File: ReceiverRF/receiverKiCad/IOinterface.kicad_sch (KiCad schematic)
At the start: 23 parts

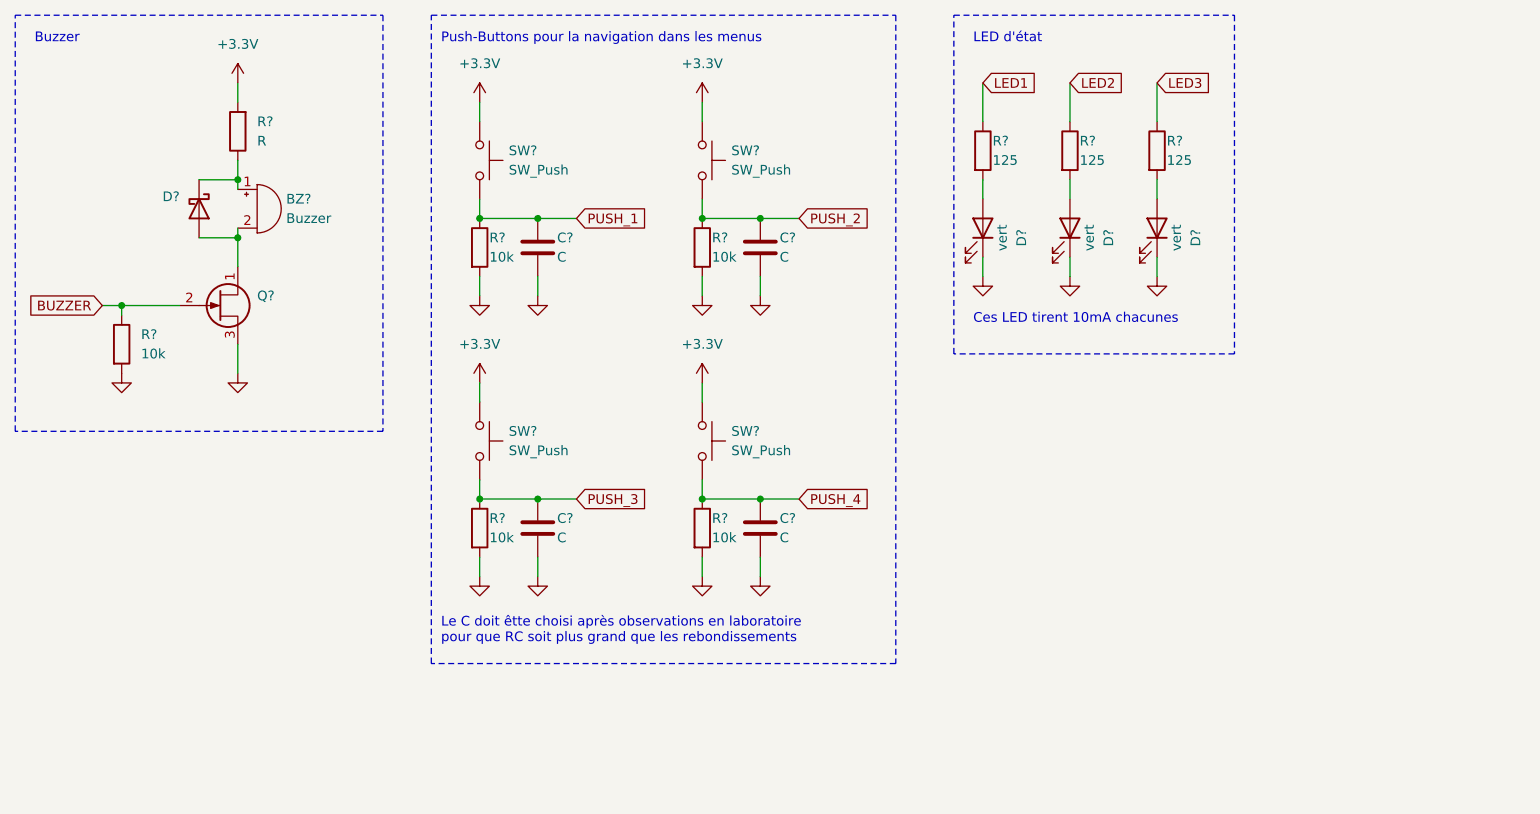
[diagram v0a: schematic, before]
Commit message: Changement régulateurs, meilleur circuit debouncing boutons, documentation
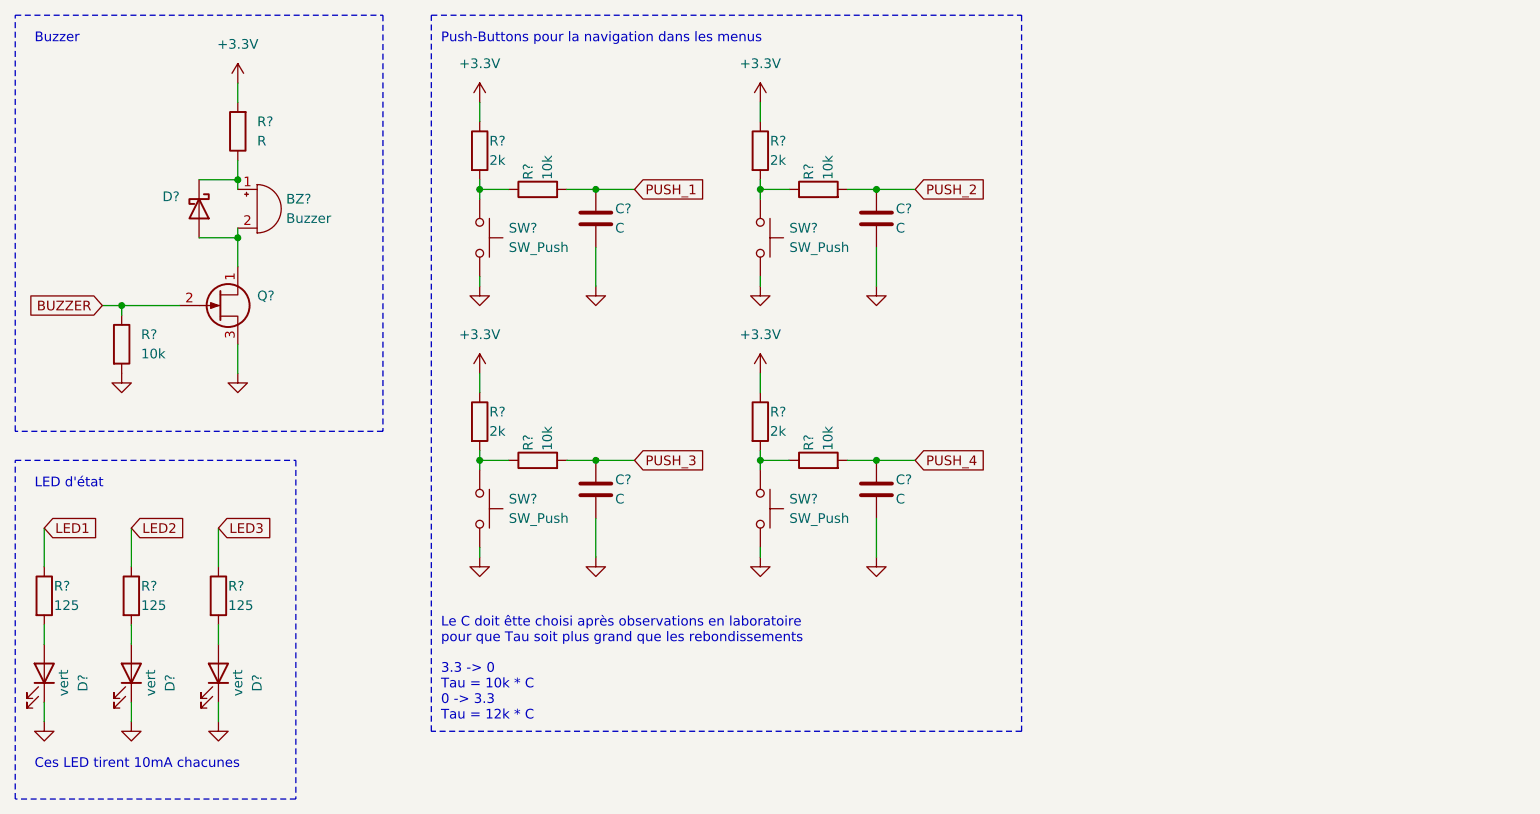
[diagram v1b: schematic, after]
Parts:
- removed C? (x3): C, symbol Device:C
- removed R? (x3): 10k, symbol Device:R
- removed SW? (x3): SW_Push, symbol Switch:SW_Push
- added C? (x3): C, symbol Device:C
- added R? (x4): 10k, symbol Device:R
- added R? (x3): 2k, symbol Device:R
- added SW? (x3): SW_Push, symbol Switch:SW_Push
- R?: value 10k -> 2k
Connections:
- net +3.3V: now also R?.1, R?.1, R?.1, R?.1; no longer SW?.1
- net GND: now also SW?.2, C?.2, C?.2, C?.2, SW?.2, SW?.2, SW?.2; no longer R?.2
- net PUSH_1: now also R?.2; no longer R?.1, SW?.2
- net PUSH_2: now also C?.1, R?.2
- net PUSH_3: now also C?.1, R?.2
- net PUSH_4: now also C?.1, R?.2
- new net: R?.1, R?.2, SW?.1 (x4)
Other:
- note added: "3.3 -> 0 Tau = 10k * C 0 -> 3.3 Tau = 12k * C"
- note added: "Le C doit êtte choisi après observations en laboratoire pour que Tau soit plus grand que les rebondissements"
- note removed: "Le C doit êtte choisi après observations en laboratoire pour que RC soit plus grand que les rebondissements"
- moved on the sheet: C?, D?, R?, SW?

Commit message: Corrige path footprints
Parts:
- BZ?: footprint footprint-receiver:SMTB-0927-TW-R_PUI -> (none)
- D? (x3): footprint footprint-receiver:LTST-C170GKT -> Footprints:LTST-C170GKT
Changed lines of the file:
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@@
 			)
 		)
-		(property "Footprint" "footprint-receiver:LTST-C170GKT"
+		(property "Footprint" "Footprints:LTST-C170GKT"
 			(at 49.53 107.95 0)
 			(effects
@@
 			)
 		)
-		(property "Footprint" "footprint-receiver:SMTB-0927-TW-R_PUI"
+		(property "Footprint" ""
 			(at 53.975 44.45 90)
 			(effects
@@
 			)
 		)
-		(property "Footprint" "footprint-receiver:LTST-C170GKT"
+		(property "Footprint" "Footprints:LTST-C170GKT"
 			(at 38.1 107.95 0)
 			(effects
@@
 			)
 		)
-		(property "Footprint" "footprint-receiver:LTST-C170GKT"
+		(property "Footprint" "Footprints:LTST-C170GKT"
 			(at 26.67 107.95 0)
 			(effects

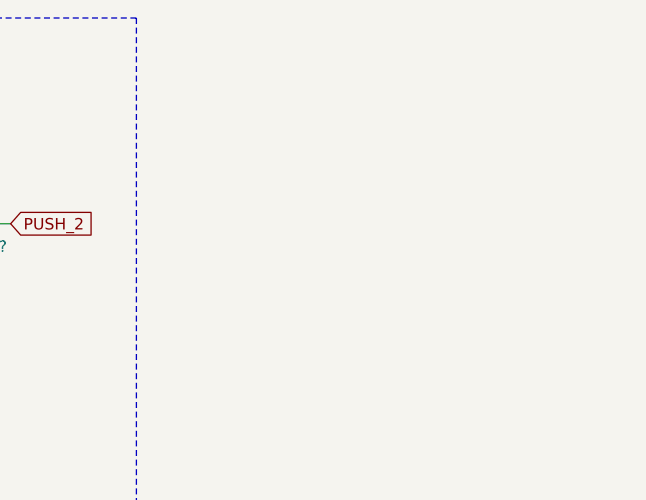
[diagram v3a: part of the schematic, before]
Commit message: Ajout footprint et circuit pour potentiomètre volume, push button, on/off switch
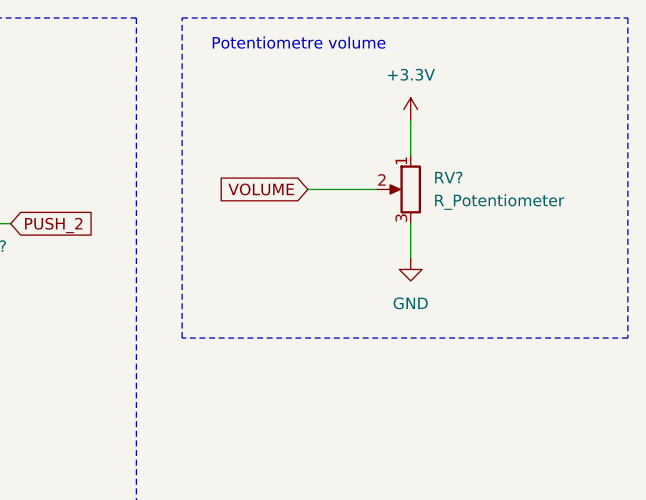
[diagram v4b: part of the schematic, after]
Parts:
- removed SW? (x3): SW_Push, symbol Switch:SW_Push
- added RV?: R_Potentiometer, Footprints:Potentiometer_Alps_RK09K_Single_Vertical, symbol Device:R_Potentiometer
- added SW? (x3): SW_Push, Footprints:SW_PUSH_6mm_H4.3mm, symbol Switch:SW_Push
- SW?: footprint (none) -> Footprints:SW_PUSH_6mm_H4.3mm
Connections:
- net +3.3V: now also RV?.1
- net GND: now also RV?.3, SW?.2, SW?.2, SW?.2
- net at R?.1, R?.2: now also SW?.1 (x3)
- new net VOLUME: RV?.2
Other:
- note added: "Potentiometre volume"

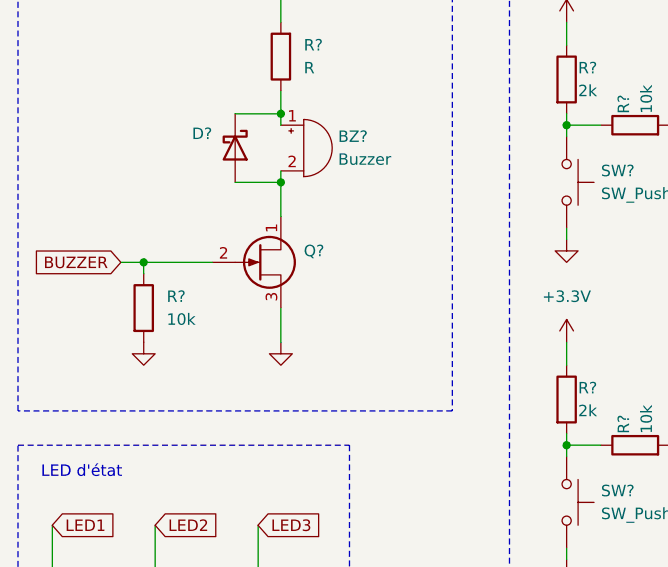
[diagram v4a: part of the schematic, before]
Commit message: Buzzer et diode. Toutes les pièces importantes sont choisies et footprint
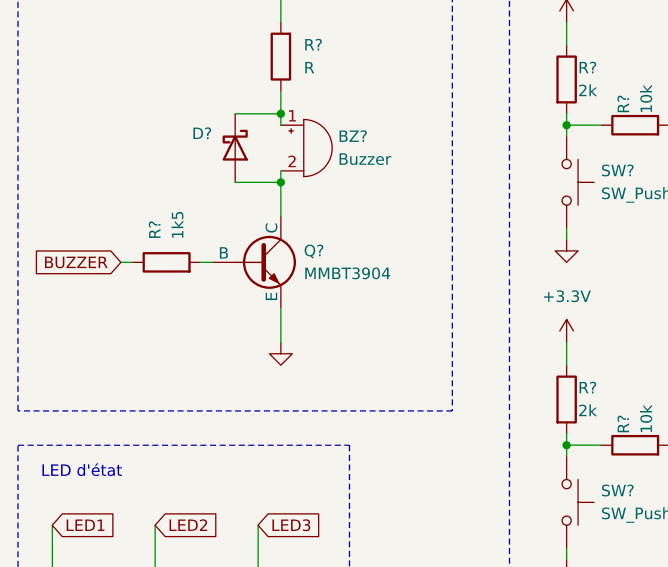
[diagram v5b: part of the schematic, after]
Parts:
- removed Q?: ~, symbol Transistor_FET:2N3819
- added Q?: MMBT3904, Footprints:SOT-23, symbol Simulation_SPICE:NPN
- BZ?: footprint (none) -> Footprints:Buzzer_D14mm_H7mm_P10mm
- D?: footprint (none) -> Diode_SMD:D_SOD-123
- R?: value 10k -> 1k5
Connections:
- net GND: now also Q?.3 (E); no longer R?.2
- net at BZ?.2 (+), D?.2 (A): now also Q?.1 (C)
- new net: Q?.2 (B), R?.2
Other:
- moved on the sheet: R?
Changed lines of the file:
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@@
 	)
 	(junction
-		(at 36.83 59.69)
-		(diameter 0)
-		(color 0 0 0 0)
-	)
-	(junction
 		(at 52.07 43.18)
 		(diameter 0)
@@
 	(wire
 		(pts
-			(xy 36.83 60.96) (xy 36.83 59.69)
-		)
-		(stroke
-			(width 0)
-			(type default)
-		)
-	)
-	(wire
-		(pts
 			(xy 173.99 40.64) (xy 181.61 40.64)
 		)
@@
 	(wire
 		(pts
-			(xy 36.83 59.69) (xy 44.45 59.69)
-		)
-		(stroke
-			(width 0)
-			(type default)
-		)
-	)
-	(wire
-		(pts
 			(xy 83.82 33.02) (xy 83.82 35.56)
 		)
@@
 	(wire
 		(pts
-			(xy 34.29 59.69) (xy 36.83 59.69)
+			(xy 99.06 44.45) (xy 104.14 44.45)
 		)
 		(stroke
@@
 	(wire
 		(pts
-			(xy 99.06 44.45) (xy 104.14 44.45)
+			(xy 120.65 68.58) (xy 120.65 71.12)
 		)
 		(stroke
@@
 	(wire
 		(pts
-			(xy 120.65 68.58) (xy 120.65 71.12)
+			(xy 83.82 44.45) (xy 83.82 45.72)
 		)
 		(stroke
@@
 	(wire
 		(pts
-			(xy 83.82 44.45) (xy 83.82 45.72)
+			(xy 135.89 52.07) (xy 135.89 57.15)
 		)
 		(stroke
@@
 	(wire
 		(pts
-			(xy 135.89 52.07) (xy 135.89 57.15)
+			(xy 99.06 52.07) (xy 99.06 57.15)
 		)
 		(stroke
@@
 	(wire
 		(pts
-			(xy 99.06 52.07) (xy 99.06 57.15)
+			(xy 34.29 59.69) (xy 35.56 59.69)
 		)
 		(stroke
@@
 	(wire
 		(pts
+			(xy 43.18 59.69) (xy 44.45 59.69)
+		)
+		(stroke
+			(width 0)
+			(type default)
+		)
+	)
+	(wire
+		(pts
 			(xy 120.65 80.01) (xy 120.65 81.28)
 		)
@@
 	)
 	(symbol
-		(lib_id "Transistor_FET:2N3819")
-		(at 49.53 59.69 0)
-		(unit 1)
-		(exclude_from_sim no)
-		(in_bom yes)
-		(on_board yes)
-		(dnp no)
-		(fields_autoplaced yes)
-		(property "Reference" "Q?"
-			(at 54.61 58.42 0)
-			(effects
-				(font
-					(size 1.27 1.27)
-				)
-				(justify left)
-			)
-		)
-		(property "Value" "~"
-			(at 54.61 60.96 0)
-			(effects
-				(font
-					(size 1.27 1.27)
-				)
-				(justify left)
-			)
-		)
-		(property "Footprint" ""
-			(at 54.61 61.595 0)
-			(effects
-				(font
-					(size 1.27 1.27)
-					(italic yes)
-				)
-				(justify left)
-				(hide yes)
-			)
-		)
-		(property "Datasheet" "https://my.centralsemi.com/datasheets/2N3819.PDF"
-			(at 49.53 59.69 0)
-			(effects
-				(font
-					(size 1.27 1.27)
-				)
-				(justify left)
-				(hide yes)
-			)
-		)
-		(property "Description" ""
-			(at 49.53 59.69 0)
-			(effects
-				(font
-					(size 1.27 1.27)
-				)
-				(hide yes)
-			)
-		)
-		(pin "1"
-		)
-		(pin "2"
-		)
-		(pin "3"
-		)
-		(instances
-			(project "receiver"
-				(path "/439ba515-58d4-4b14-87ab-b438dcf423a5/4d4f24f8-ecba-4dd7-9441-941d52592651"
-					(reference "Q?")
-					(unit 1)
-				)
-			)
-		)
-	)
-	(symbol
 		(lib_id "Device:R")
 		(at 52.07 36.83 180)
@@
 			)
 		)
-		(property "Footprint" ""
+		(property "Footprint" "Footprints:Buzzer_D14mm_H7mm_P10mm"
 			(at 53.975 44.45 90)
 			(effects
@@
 			)
 		)
-		(property "Datasheet" "~"
+		(property "Datasheet" "https://www.digikey.com/en/products/detail/pui-audio-inc/SMTB-0927-TW-R/13165907"
 			(at 53.975 44.45 90)
 			(effects
@@
 	(symbol
 		(lib_id "power:GND")
-		(at 36.83 68.58 0)
+		(at 83.82 57.15 0)
 		(unit 1)
 		(exclude_from_sim no)
@@
 		(dnp no)
 		(fields_autoplaced yes)
-		(property "Reference" "#PWR041"
-			(at 36.83 74.93 0)
+		(property "Reference" "#PWR043"
+			(at 83.82 63.5 0)
 			(effects
 				(font
@@
 		)
 		(property "Value" "GND"
-			(at 36.83 73.66 0)
+			(at 83.82 62.23 0)
 			(effects
 				(font
@@
 		)
 		(property "Footprint" ""
-			(at 36.83 68.58 0)
+			(at 83.82 57.15 0)
 			(effects
 				(font
@@
 		)
 		(property "Datasheet" ""
-			(at 36.83 68.58 0)
+			(at 83.82 57.15 0)
 			(effects
 				(font
@@
 		)
 		(property "Description" ""
-			(at 36.83 68.58 0)
+			(at 83.82 57.15 0)
 			(effects
 				(font
@@
 			(project "receiver"
 				(path "/439ba515-58d4-4b14-87ab-b438dcf423a5/4d4f24f8-ecba-4dd7-9441-941d52592651"
-					(reference "#PWR041")
+					(reference "#PWR043")
 					(unit 1)
 				)
@@
 	)
 	(symbol
-		(lib_id "power:GND")
-		(at 83.82 57.15 0)
+		(lib_id "Simulation_SPICE:NPN")
+		(at 49.53 59.69 0)
 		(unit 1)
 		(exclude_from_sim no)
@@
 		(dnp no)
 		(fields_autoplaced yes)
-		(property "Reference" "#PWR043"
-			(at 83.82 63.5 0)
+		(property "Reference" "Q?"
+			(at 54.61 58.4199 0)
+			(effects
+				(font
+					(size 1.27 1.27)
+				)
+				(justify left)
+			)
+		)
+		(property "Value" "MMBT3904"
+			(at 54.61 60.9599 0)
+			(effects
+				(font
+					(size 1.27 1.27)
+				)
+				(justify left)
+			)
+		)
+		(property "Footprint" "Footprints:SOT-23"
+			(at 113.03 59.69 0)
 			(effects
 				(font
@@
 			)
 		)
-		(property "Value" "GND"
-			(at 83.82 62.23 0)
+		(property "Datasheet" "https://www.digikey.ca/en/products/detail/onsemi/MMBT3904LT1G/1139813"
+			(at 113.03 59.69 0)
 			(effects
 				(font
@@
 			)
 		)
-		(property "Footprint" ""
-			(at 83.82 57.15 0)
+		(property "Description" "Bipolar transistor symbol for simulation only, substrate tied to the emitter"
+			(at 49.53 59.69 0)
 			(effects
 				(font
@@
 			)
 		)
-		(property "Datasheet" ""
-			(at 83.82 57.15 0)
+		(property "Sim.Device" "NPN"
+			(at 49.53 59.69 0)
 			(effects
 				(font
@@
 			)
 		)
-		(property "Description" ""
-			(at 83.82 57.15 0)
+		(property "Sim.Type" "GUMMELPOON"
+			(at 49.53 59.69 0)
+			(effects
+				(font
+					(size 1.27 1.27)
+				)
+				(hide yes)
+			)
+		)
+		(property "Sim.Pins" "1=C 2=B 3=E"
+			(at 49.53 59.69 0)
 			(effects
 				(font
@@
 			)
 		)
+		(pin "3"
+		)
 		(pin "1"
 		)
+		(pin "2"
+		)
 		(instances
-			(project "receiver"
+			(project ""
 				(path "/439ba515-58d4-4b14-87ab-b438dcf423a5/4d4f24f8-ecba-4dd7-9441-941d52592651"
-					(reference "#PWR043")
+					(reference "Q?")
 					(unit 1)
 				)
@@
 	(symbol
 		(lib_id "Device:R")
-		(at 36.83 64.77 0)
+		(at 39.37 59.69 90)
 		(unit 1)
 		(exclude_from_sim no)
@@
 		(on_board yes)
 		(dnp no)
-		(fields_autoplaced yes)
 		(property "Reference" "R?"
-			(at 39.37 63.5 0)
+			(at 38.1 57.15 0)
 			(effects
 				(font
@@
 			)
 		)
-		(property "Value" "10k"
-			(at 39.37 66.04 0)
+		(property "Value" "1k5"
+			(at 40.64 57.15 0)
 			(effects
 				(font
@@
 		)
 		(property "Footprint" ""
-			(at 35.052 64.77 90)
+			(at 39.37 61.468 90)
 			(effects
 				(font
@@
 		)
 		(property "Datasheet" "~"
-			(at 36.83 64.77 0)
+			(at 39.37 59.69 0)
 			(effects
 				(font
@@
 		)
 		(property "Description" ""
-			(at 36.83 64.77 0)
+			(at 39.37 59.69 0)
 			(effects
 				(font
@@
 			)
 		)
-		(property "Footprint" ""
+		(property "Footprint" "Diode_SMD:D_SOD-123"
 			(at 42.545 46.99 0)
 			(effects
@@
 			)
 		)
-		(property "Datasheet" "https://www.microsemi.com/document-portal/doc_download/131890-lds-0040-1-datasheet"
+		(property "Datasheet" "https://www.digikey.ca/en/products/detail/onsemi/BAT54T1G/918319"
 			(at 46.99 46.99 0)
 			(effects

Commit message: Identifiants des symboles
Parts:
- BUZ_R1: renamed from R?; value R -> 30R
- gave numbers to parts that had none: 27
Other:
- moved on the sheet: BUT_C1, BUT_C2, BUT_C3, BUT_C4, BUT_R2, BUT_R3, BUT_R4, BUT_R6, BUT_R7, BUT_R8, RV1, SW2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

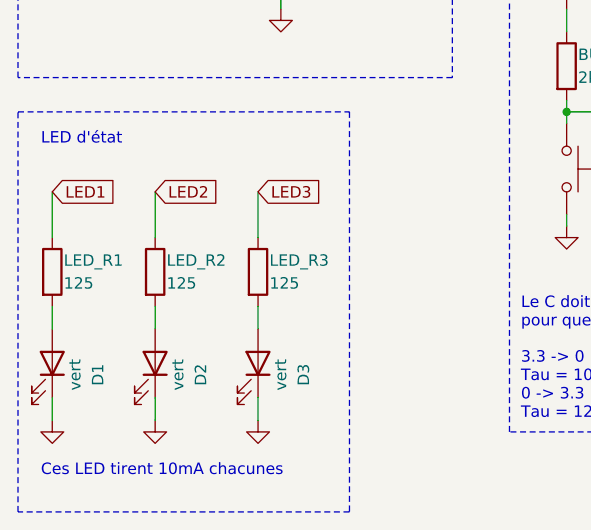
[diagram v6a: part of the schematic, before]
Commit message: Footprint et choix composantes mineures (résistances et condo)
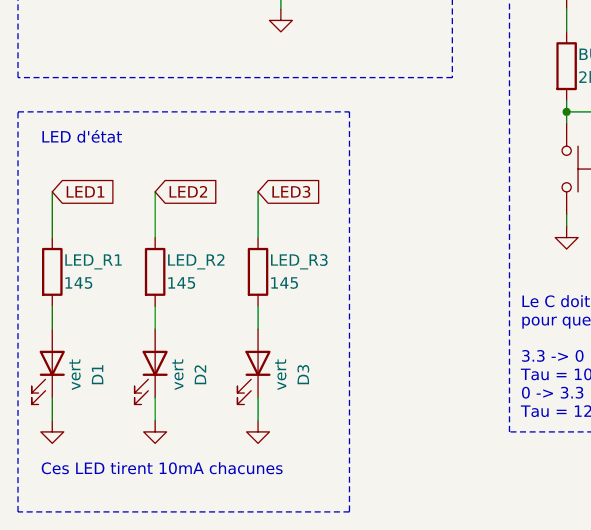
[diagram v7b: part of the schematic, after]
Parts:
- BUT_C1, BUT_C2, BUT_C3, BUT_C4: footprint (none) -> Capacitor_SMD:C_0402_1005Metric
- BUT_R1, BUT_R2, BUT_R5, BUT_R6, BUZ_R1, BUZ_R2: footprint (none) -> Resistor_SMD:R_1206_3216Metric
- BUT_R3, BUT_R4, BUT_R7, BUT_R8: footprint (none) -> Resistor_SMD:R_0402_1005Metric
- LED_R1, LED_R2, LED_R3: value 125 -> 145; footprint (none) -> Resistor_SMD:R_1206_3216Metric
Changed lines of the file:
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@@
 			)
 		)
-		(property "Footprint" ""
+		(property "Footprint" "Resistor_SMD:R_0402_1005Metric"
 			(at 138.43 46.228 90)
 			(effects
@@
 			)
 		)
-		(property "Footprint" ""
+		(property "Footprint" "Resistor_SMD:R_1206_3216Metric"
 			(at 53.848 36.83 90)
 			(effects
@@
 			)
 		)
-		(property "Footprint" ""
+		(property "Footprint" "Capacitor_SMD:C_0402_1005Metric"
 			(at 105.1052 54.61 0)
 			(effects
@@
 			)
 		)
-		(property "Value" "125"
+		(property "Value" "145"
 			(at 39.37 99.06 0)
 			(effects
@@
 			)
 		)
-		(property "Footprint" ""
+		(property "Footprint" "Resistor_SMD:R_1206_3216Metric"
 			(at 36.322 97.79 90)
 			(effects
@@
 			)
 		)
-		(property "Footprint" ""
+		(property "Footprint" "Resistor_SMD:R_0402_1005Metric"
 			(at 96.52 81.788 90)
 			(effects
@@
 			)
 		)
-		(property "Footprint" ""
+		(property "Footprint" "Resistor_SMD:R_0402_1005Metric"
 			(at 138.43 81.788 90)
 			(effects
@@
 			)
 		)
-		(property "Footprint" ""
+		(property "Footprint" "Capacitor_SMD:C_0402_1005Metric"
 			(at 147.0152 90.17 0)
 			(effects
@@
 			)
 		)
-		(property "Footprint" ""
+		(property "Footprint" "Resistor_SMD:R_0402_1005Metric"
 			(at 96.52 46.228 90)
 			(effects
@@
 			)
 		)
-		(property "Footprint" ""
+		(property "Footprint" "Resistor_SMD:R_1206_3216Metric"
 			(at 39.37 61.468 90)
 			(effects
@@
 			)
 		)
-		(property "Footprint" ""
+		(property "Footprint" "Resistor_SMD:R_1206_3216Metric"
 			(at 122.682 39.37 90)
 			(effects
@@
 			)
 		)
-		(property "Footprint" ""
+		(property "Footprint" "Capacitor_SMD:C_0402_1005Metric"
 			(at 147.0152 54.61 0)
 			(effects
@@
 			)
 		)
-		(property "Footprint" ""
+		(property "Footprint" "Resistor_SMD:R_1206_3216Metric"
 			(at 82.042 74.93 90)
 			(effects
@@
 			)
 		)
-		(property "Footprint" ""
+		(property "Footprint" "Resistor_SMD:R_1206_3216Metric"
 			(at 122.682 74.93 90)
 			(effects
@@
 			)
 		)
-		(property "Value" "125"
+		(property "Value" "145"
 			(at 50.8 99.06 0)
 			(effects
@@
 			)
 		)
-		(property "Footprint" ""
+		(property "Footprint" "Resistor_SMD:R_1206_3216Metric"
 			(at 47.752 97.79 90)
 			(effects
@@
 			)
 		)
-		(property "Footprint" ""
+		(property "Footprint" "Capacitor_SMD:C_0402_1005Metric"
 			(at 105.1052 90.17 0)
 			(effects
@@
 			)
 		)
-		(property "Value" "125"
+		(property "Value" "145"
 			(at 27.94 99.06 0)
 			(effects
@@
 			)
 		)
-		(property "Footprint" ""
+		(property "Footprint" "Resistor_SMD:R_1206_3216Metric"
 			(at 24.892 97.79 90)
 			(effects
@@
 			)
 		)
-		(property "Footprint" ""
+		(property "Footprint" "Resistor_SMD:R_1206_3216Metric"
 			(at 82.042 39.37 90)
 			(effects
